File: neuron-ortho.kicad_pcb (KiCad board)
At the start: 2 copper layers, 228.6 x 77.8 mm, 134 parts, among them J1 USB_C_Receptacle_USB2.0, J2 Conn_01x04_Male, J3 Conn_01x06_Male, Q1 DTC123J, SW1 SW_Push, U1 STM32F303C6Tx, U2 NCP1117-3.3_SOT223, U3 USBLC6-2SC6, Y1 8MHz

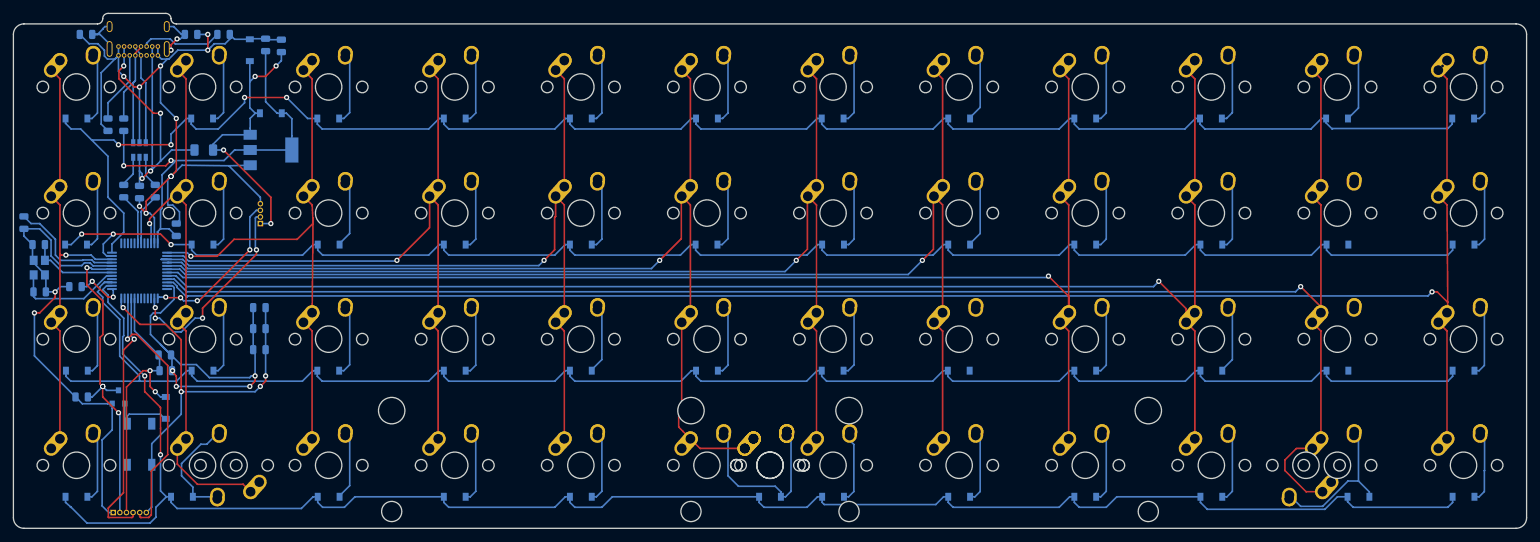
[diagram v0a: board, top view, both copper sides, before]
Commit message: Deleted traces, move component placing
Got some tips from Xelus and started over with component placement. New traces next
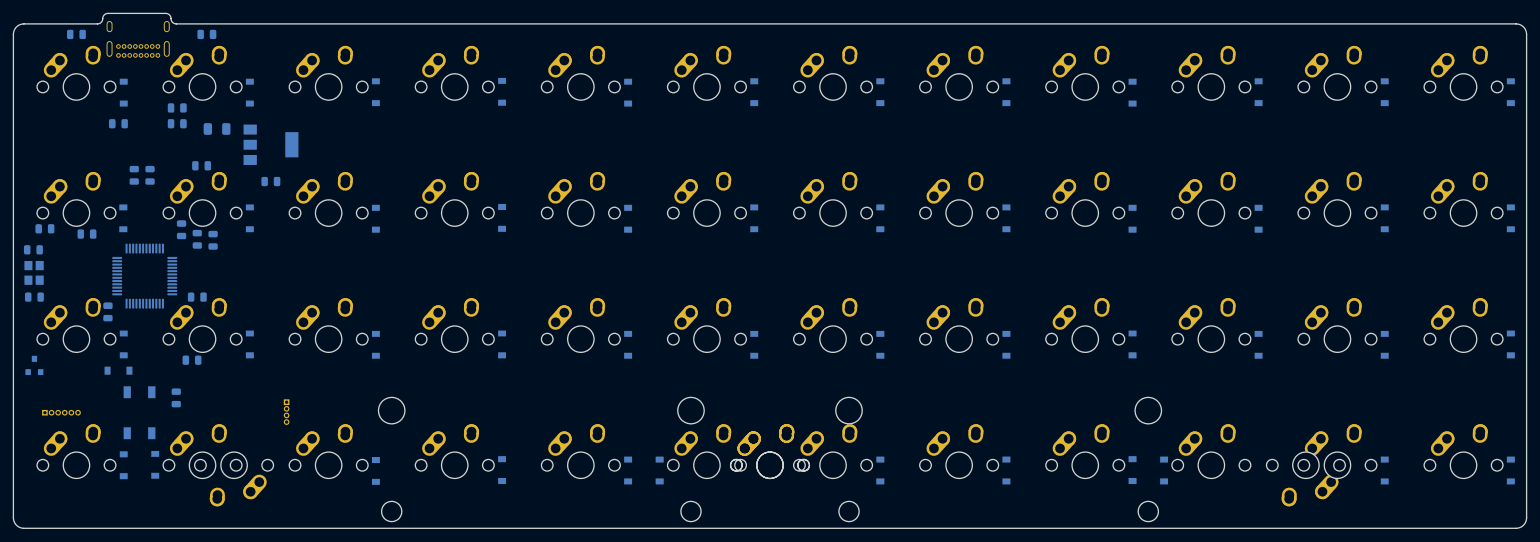
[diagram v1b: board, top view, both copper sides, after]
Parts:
- removed CUSB1: 4.7n, Capacitor_SMD:C_0805_2012Metric
- removed D1: 1N4007, Diode_SMD:D_SOD-123
- removed DF1: RB060M-60TR, Diode_SMD:D_SOD-123
- removed U3: USBLC6-2SC6, Package_TO_SOT_SMD:SOT-23-6
- C10, C9: value 100n -> 10u
- moved C1 28.5 mm to (59.5, 96.8), turned to 180 degrees
- moved J2 27.3 mm to (73.0, 112.7), turned to 180 degrees
- moved C11 26.0 mm to (36.5, 86.5)
- moved C9 21.8 mm to (60.2, 77.0), turned to 180 degrees
- moved C10 20.7 mm to (70.6, 79.4), turned to 180 degrees
- moved C3 19.0 mm to (57.1, 86.7), turned to 270 degrees
- moved J3 18.3 mm to (36.5, 114.3)
- moved R4 18.3 mm to (61.0, 57.1), turned to 180 degrees
- moved C5 17.9 mm to (61.9, 88.2), turned to 90 degrees
- moved C7 17.3 mm to (41.3, 57.1), turned to 180 degrees
- moved DX42 17.1 mm to (129.4, 123.0), turned to 90 degrees
- moved C6 16.1 mm to (46.0, 99.1), turned to 90 degrees
- moved C4 13.9 mm to (59.5, 88.1), turned to 270 degrees
- moved Q1 13.6 mm to (34.9, 107.2)
- moved R2 13.1 mm to (56.5, 68.3)
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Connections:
- R6 pad 1: Net-(R6-Pad1) -> D+Bus
- R7 pad 1: Net-(R7-Pad1) -> D-Bus
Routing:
- net ROW3: track 270.3 -> 0.00 mm, vias 2 -> 0
- net +5V: track 268.1 -> 0.00 mm, vias 16 -> 0
- net ROW0: track 255.7 -> 0.00 mm, vias 4 -> 0
- net COL11: track 252.8 -> 0.00 mm, vias 2 -> 0
- net ROW2: track 250.2 -> 0.00 mm
- net COL10: track 245.4 -> 0.00 mm, vias 1 -> 0
- net ROW1: track 234.5 -> 0.00 mm, vias 3 -> 0
- net COL9: track 213.1 -> 0.00 mm, vias 1 -> 0
- net COL8: track 196.7 -> 0.00 mm, vias 1 -> 0
- net COL7: track 180.1 -> 0.00 mm, vias 1 -> 0
- net COL6: track 160.9 -> 0.00 mm, vias 1 -> 0
- net 3.3V: track 155.7 -> 0.00 mm, vias 8 -> 0
- net COL5: track 150.0 -> 0.00 mm, vias 1 -> 0
- net COL4: track 124.2 -> 0.00 mm, vias 1 -> 0
- net COL3: track 101.2 -> 0.00 mm, vias 1 -> 0
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
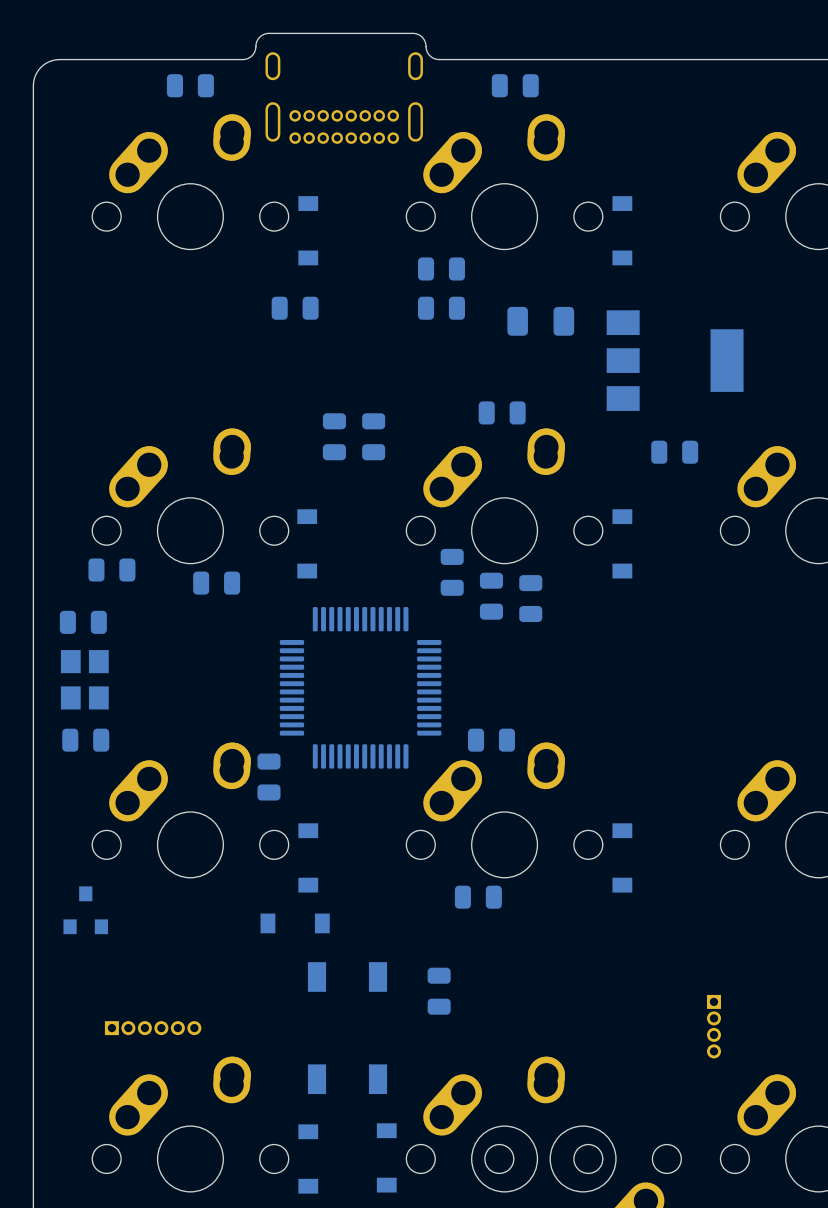
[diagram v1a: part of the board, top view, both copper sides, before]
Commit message: Finished non-switch matrix traces
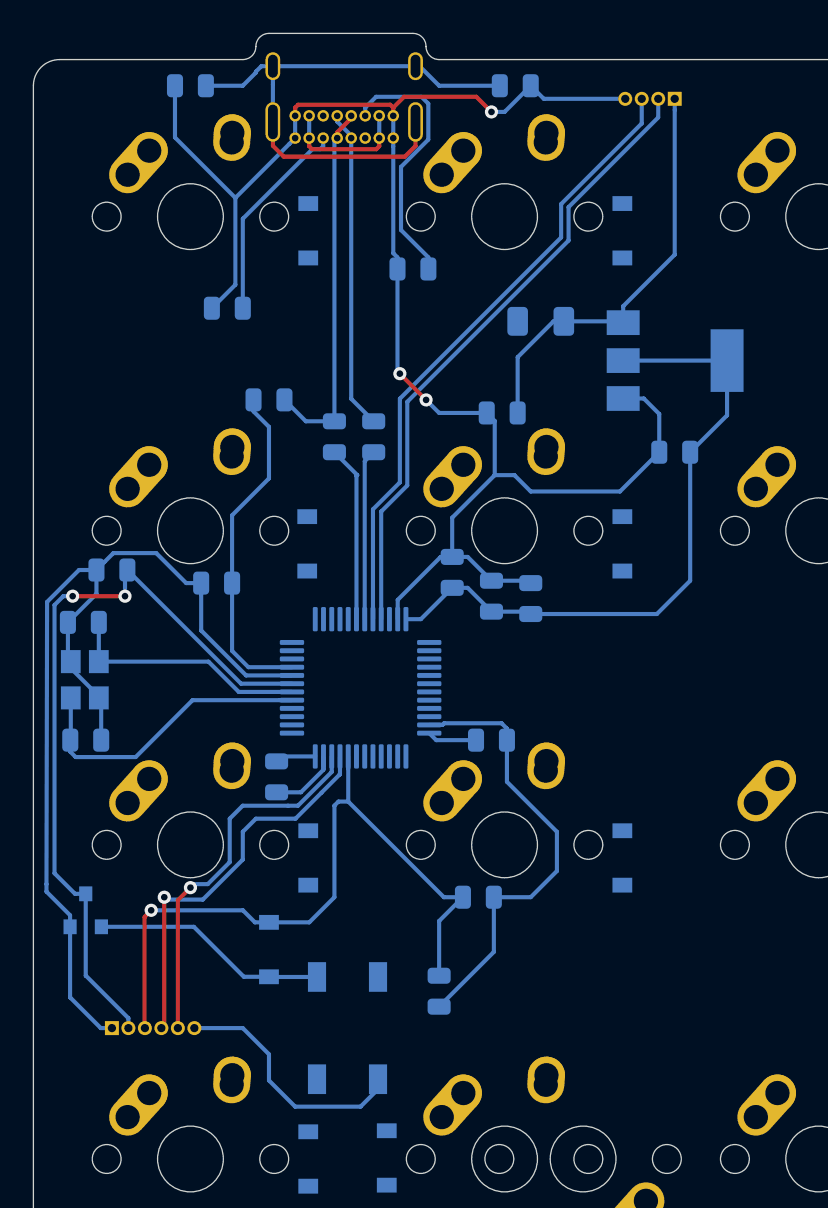
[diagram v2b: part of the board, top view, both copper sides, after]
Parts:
- moved J2 54.8 mm to (70.6, 57.9), turned to 90 degrees
- moved R1 13.0 mm to (43.5, 70.6), turned to 0 degrees
- moved R3 5.78 mm to (46.0, 76.2), turned to 0 degrees
- moved D3 2.25 mm to (46.0, 109.5), turned to 270 degrees
- moved R2 1.73 mm to (54.8, 68.3), turned to 0 degrees
- moved C6 0.46 mm to (46.5, 99.1)
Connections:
- U1 pad 20: Net-(U1-Pad20) -> SCL
- U1 pad 21: Net-(U1-Pad21) -> SDA
- U1 pad 37: SCL -> Net-(U1-Pad37)
- U1 pad 38: SDA -> Net-(U1-Pad38)
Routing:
- net +5V: track 0.00 -> 196.3 mm, vias 0 -> 3
- net 3.3V: track 0.00 -> 81.2 mm
- net NRST: track 0.00 -> 46.9 mm, vias 0 -> 2
- net BOOT0: track 0.00 -> 43.3 mm, vias 0 -> 1
- net SDA: track 0.00 -> 38.5 mm
- net SCL: track 0.00 -> 38.3 mm
- net Net-(C7-Pad1): track 0.00 -> 34.3 mm
- net 5V: track 0.00 -> 25.6 mm
- net SWDIO: track 0.00 -> 23.9 mm, vias 0 -> 1
- net SWCLK: track 0.00 -> 23.0 mm, vias 0 -> 1
- net D+Bus: track 0.00 -> 22.5 mm
- net D-Bus: track 0.00 -> 19.4 mm
- net XTAL1: track 0.00 -> 18.3 mm
- net Net-(J1-PadB5): track 0.00 -> 16.2 mm
- net XTAL2: track 0.00 -> 14.9 mm
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
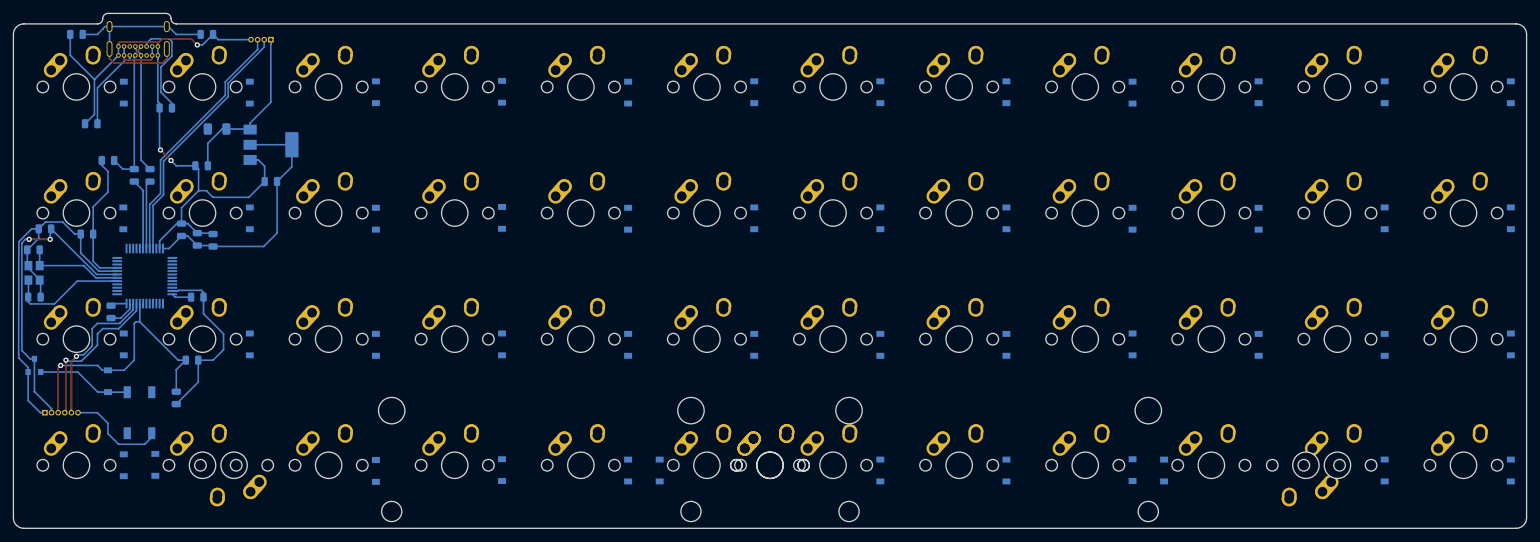
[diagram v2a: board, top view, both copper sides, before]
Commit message: Switch matrix traces done
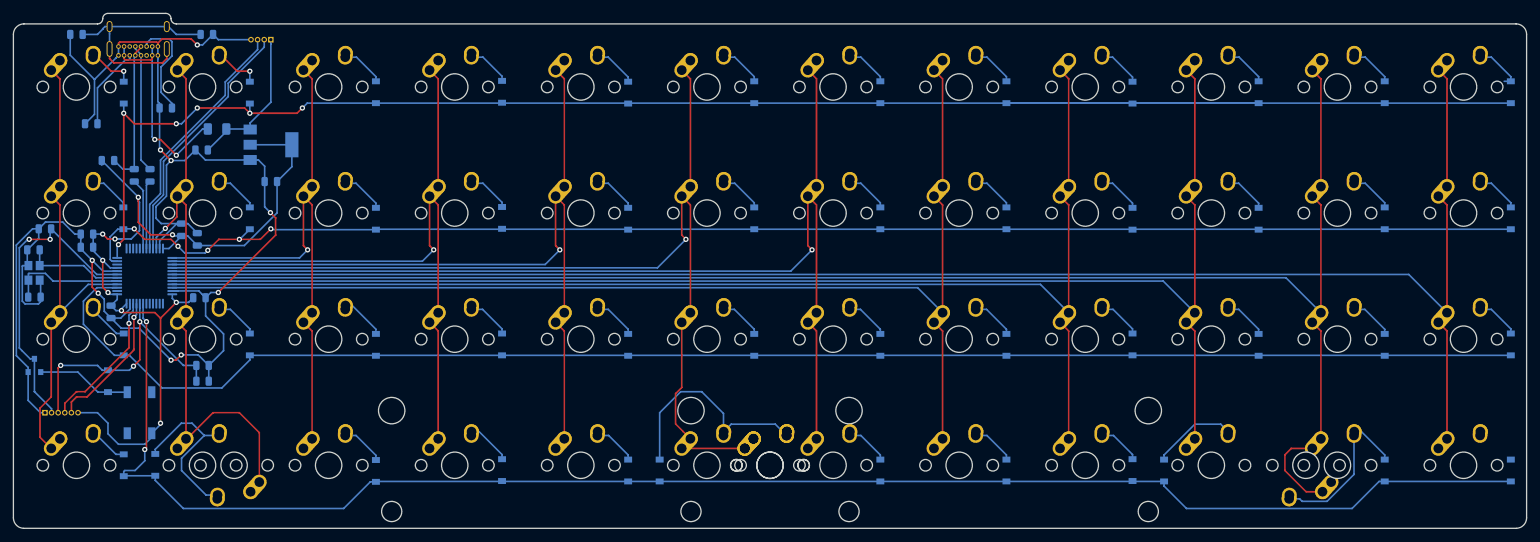
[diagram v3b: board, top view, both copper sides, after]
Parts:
- moved C5 19.1 mm to (42.9, 89.3), turned to 180 degrees
- moved C12 4.70 mm to (60.3, 109.5), turned to 0 degrees
- moved C9 2.38 mm to (60.2, 74.6)
- moved R8 1.77 mm to (60.3, 107.2)
- moved C1 0.33 mm to (59.9, 96.9)
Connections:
- U1 pad 10: COL0 -> Net-(U1-Pad10)
- U1 pad 2: ROW3 -> Net-(U1-Pad2)
- U1 pad 30: COL7 -> COL11
- U1 pad 31: COL8 -> COL10
- U1 pad 33: COL10 -> COL8
- U1 pad 34: COL11 -> COL7
- U1 pad 4: Net-(U1-Pad4) -> COL0
- U1 pad 43: Net-(U1-Pad43) -> ROW3
- U1 pad 45: SWDIO -> SWCLK
- U1 pad 46: SWCLK -> SWDIO
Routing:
- net ROW0: track 0.00 -> 275.5 mm, vias 0 -> 6
- net COL11: track 0.00 -> 253.4 mm
- net COL10: track 0.00 -> 250.0 mm
- net ROW3: track 0.00 -> 246.1 mm, vias 0 -> 2
- net ROW2: track 0.00 -> 231.5 mm
- net ROW1: track 0.00 -> 222.0 mm, vias 0 -> 5
- net COL9: track 0.00 -> 210.8 mm
- net COL8: track 0.00 -> 193.6 mm
- net COL7: track 0.00 -> 174.3 mm
- net COL6: track 0.00 -> 166.7 mm, vias 0 -> 1
- net COL5: track 0.00 -> 152.8 mm, vias 0 -> 1
- net COL4: track 0.00 -> 124.2 mm, vias 0 -> 1
- net COL3: track 0.00 -> 103.0 mm, vias 0 -> 1
- net COL2: track 0.00 -> 87.7 mm, vias 0 -> 1
- net COL1: track 0.00 -> 86.9 mm, vias 0 -> 1
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
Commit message: Tidied traces, added logo
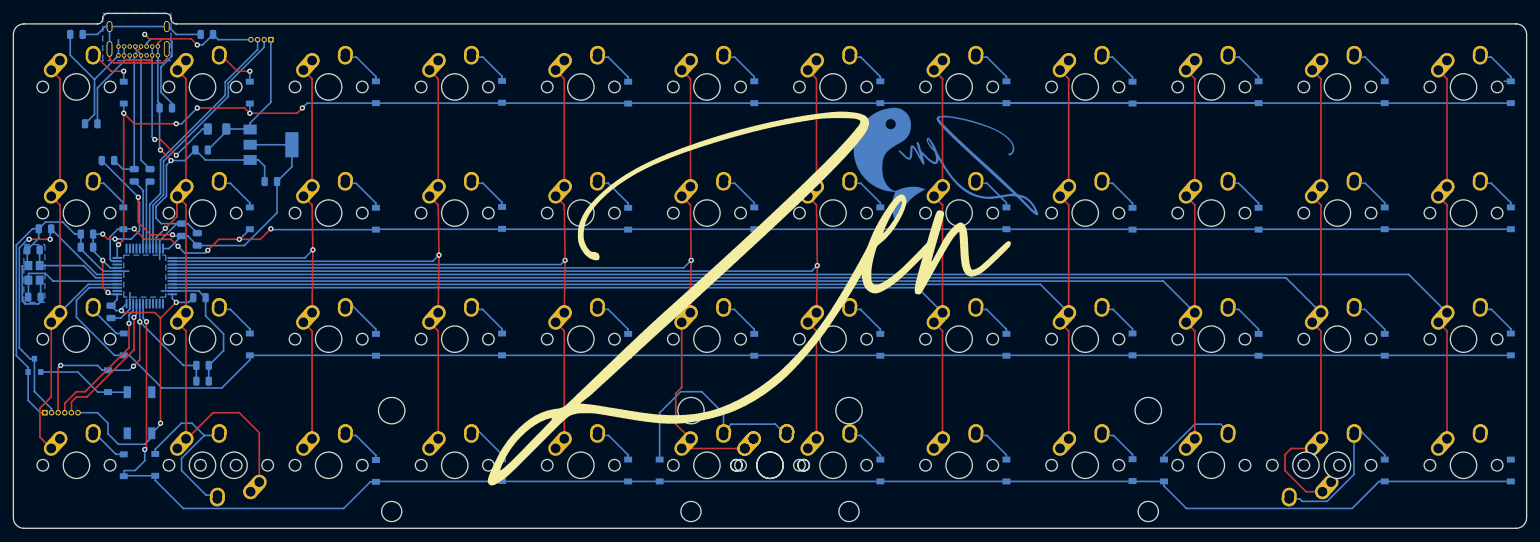
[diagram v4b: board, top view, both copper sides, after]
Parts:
- added G***: LOGO, random-keyboard-parts:PCBlogoZen1, F.Cu at (135.6, 94.2)
- added G***, G2: LOGO, random-keyboard-parts:PCBlogoZen, B.Cu at (178.0, 76.2)
- added G3 (x2): LOGO, random-keyboard-parts:PCBlogoKoiFlipped, B.Cu at (164.0, 77.0)
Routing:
- net +5V: track 248.9 -> 201.4 mm, vias 9 -> 4
- net COL6: track 166.7 -> 158.2 mm
- net COL4: track 124.2 -> 116.0 mm
- net COL3: track 103.0 -> 95.1 mm
- net COL2: track 87.7 -> 80.1 mm
- net COL5: track 152.8 -> 145.5 mm
- net ROW2: track 231.5 -> 233.1 mm
- added copper zone on B.Cu, net +5V
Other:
- board text added: "GND NRST BOOT0 SWDIO SWCLK 3.3V"
- board text added: "GND SCL SDA 5V"

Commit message: Updated pin out footprint
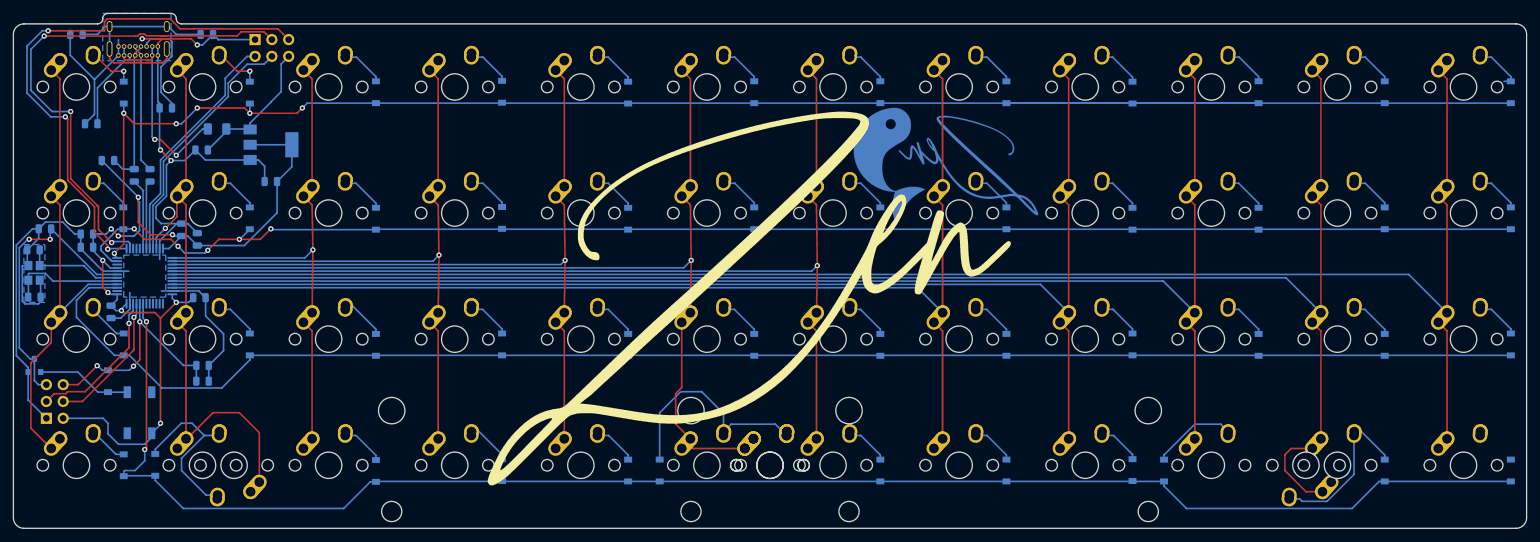
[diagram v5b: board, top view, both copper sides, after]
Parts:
- J2: value Conn_01x04_Male -> Conn_01x06_Male; footprint Connector_PinSocket_1.00mm:PinSocket_1x04_P1.00mm_Vertical -> random-keyboard-parts:Reset_Pretty
- J3: footprint Connector_PinSocket_1.00mm:PinSocket_1x06_P1.00mm_Vertical -> random-keyboard-parts:Reset_Pretty
- moved J3 2.26 mm to (38.0, 112.6), turned to 180 degrees
- moved J2 1.27 mm to (70.8, 59.2)
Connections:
- J2 pad 2: SDA -> Extra1
- J2 pad 3: SCL -> SDA
- J2 pad 4: +5V -> Extra2
- J3 pad 1: +5V -> BOOT0
- J3 pad 3: BOOT0 -> SWCLK
- J3 pad 5: SWCLK -> 3.3V
- J3 pad 6: 3.3V -> +5V
- U1 pad 13: Net-(U1-Pad13) -> Extra1
- U1 pad 14: Net-(U1-Pad14) -> Extra2
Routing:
- net Extra1: track 0.00 -> 83.2 mm, vias 0 -> 3
- net Extra2: track 0.00 -> 78.3 mm, vias 0 -> 3
- net BOOT0: track 42.4 -> 35.9 mm
- net NRST: track 47.0 -> 43.1 mm
- net 3.3V: track 139.0 -> 141.2 mm
- net SCL: track 38.3 -> 36.3 mm
- net ROW1: track 222.0 -> 223.5 mm
- net 5V: track 22.8 -> 21.4 mm
- net +5V: track 201.4 -> 202.7 mm
- net COL0: track 69.2 -> 70.3 mm
- net SWDIO: track 21.8 -> 22.8 mm
- net SDA: track 38.5 -> 38.0 mm
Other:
- outline, holes or cut-outs redrawn
- board text removed: "GND NRST BOOT0 SWDIO SWCLK 3.3V"
- board text removed: "GND SCL SDA 5V"

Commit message: Added missing trace
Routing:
- net Net-(DX48-Pad2): track 0.00 -> 6.56 mm
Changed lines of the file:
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@@
     (thickness 1.6)
     (drawings 15)
-    (tracks 799)
+    (tracks 802)
     (zones 0)
     (modules 135)
@@
   (segment (start 226.433491 127.687501) (end 226.06349 127.3175) (width 0.25) (layer B.Cu) (net 61))
   (segment (start 234.275 117.7375) (end 234.275 123.621002) (width 0.25) (layer B.Cu) (net 61))
+  (segment (start 255.025 117.7375) (end 253.325 117.7375) (width 0.25) (layer B.Cu) (net 62))
+  (segment (start 257.96875 120.68125) (end 255.025 117.7375) (width 0.25) (layer B.Cu) (net 62))
+  (segment (start 257.96875 121.38125) (end 257.96875 120.68125) (width 0.25) (layer B.Cu) (net 62))
   (segment (start 50.00625 60.49375) (end 50.175 60.325) (width 0.25) (layer B.Cu) (net 63))
   (segment (start 50.00625 77.5) (end 50.00625 60.49375) (width 0.25) (layer B.Cu) (net 63))
